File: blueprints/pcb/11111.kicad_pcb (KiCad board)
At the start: 2 copper layers, 128 parts, among them J1 MJ-4PP-9, J2 MJ-4PP-9, SW1 SW_Push, SW10 SW_Push, SW11 SW_Push, SW12 SW_Push, SW13 SW_Push, SW14 SW_Push, SW15 SW_Push, SW16 SW_Push, SW17 SW_Push, SW18 SW_Push, SW19 SW_Push, SW2 SW_Push, SW20 SW_Push, SW21 SW_Push, SW22 SW_Push, SW23 SW_Push, SW24 SW_Push, SW25 SW_Push, SW26 SW_Push, SW27 SW_Push, SW28 SW_Push, SW29 SW_Push, SW3 SW_Push, SW30 SW_Push, SW31 SW_Push, SW32 SW_Push, SW33 SW_Push, SW34 SW_Push, SW35 SW_Push, SW36 SW_Push, SW37 SW_Push, SW38 SW_Push, SW39 SW_Push, SW4 SW_Push, SW40 SW_Push, SW41 SW_Push, SW42 SW_Push, SW43 SW_Push, SW44 SW_Push, SW45 SW_Push, SW46 SW_Push, SW47 SW_Push, SW48 SW_Push, SW49 SW_Push, SW5 SW_Push, SW50 SW_Push, SW51 SW_Push, SW52 SW_Push, SW53 SW_Push, SW54 SW_Push, SW55 SW_Push, SW56 SW_Push, SW57 SW_Push, SW58 SW_Push, SW59 SW_Push, SW6 SW_Push, SW60 SW_Push, SW61 SW_Push, SW62 SW_Push, SW7 SW_Push, SW8 SW_Push, SW9 SW_Push

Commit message: edit PCB
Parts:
- moved SW28 267.6 mm to (281.9, 39.4)
- moved D28 259.7 mm to (269.8, 44.5), turned to 90 degrees
- moved D41 237.2 mm to (250.8, 63.5), turned to 90 degrees
- moved SW14 215.3 mm to (281.9, 20.3)
- moved SW56 211.5 mm to (281.9, 77.5)
- moved D10 200.0 mm to (193.6, 25.4), turned to 90 degrees
- moved D12 197.9 mm to (231.8, 26.3), turned to 90 degrees
- moved D14 195.5 mm to (270.2, 27.8), turned to 90 degrees
- moved D13 193.3 mm to (250.8, 25.4), turned to 90 degrees
- moved SW40 192.9 mm to (243.8, 58.4)
- moved SW13 192.6 mm to (262.8, 20.3)
- moved D24 185.7 mm to (193.7, 44.5), turned to 90 degrees
- moved D11 182.1 mm to (212.9, 26.3), turned to 90 degrees
- moved D39 181.1 mm to (212.7, 63.5), turned to 90 degrees
- moved D38 180.1 mm to (193.7, 63.5), turned to 90 degrees
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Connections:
- SW60 pad 1: Col11 -> Col7
- SW61 pad 1: Col12 -> Col8
- SW62 pad 1: Col13 -> Col9

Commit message: edit PCB
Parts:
- moved RZ2 57.6 mm to (213.2, 48.0), turned to 90 degrees
- moved D62 56.0 mm to (239.7, 123.2), turned to 180 degrees
- moved D61 55.4 mm to (220.6, 123.2), turned to 180 degrees
- moved D22 54.3 mm to (205.8, 66.4), turned to 180 degrees
- moved D60 51.7 mm to (201.9, 123.2), turned to 180 degrees
- moved D36 51.3 mm to (201.9, 85.5), turned to 180 degrees
- moved D41 51.2 mm to (297.2, 85.1), turned to 180 degrees
- moved D42 51.2 mm to (316.3, 85.1), turned to 180 degrees
- moved D37 51.0 mm to (220.6, 85.5), turned to 180 degrees
- moved D23 51.0 mm to (220.6, 66.4), turned to 180 degrees
- moved D52 51.0 mm to (239.7, 104.5), turned to 180 degrees
- moved D50 51.0 mm to (201.6, 104.5), turned to 180 degrees
- moved D24 51.0 mm to (239.7, 66.4), turned to 180 degrees
- moved D51 51.0 mm to (220.6, 104.5), turned to 180 degrees
- moved D53 51.0 mm to (258.7, 104.5), turned to 180 degrees
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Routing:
- net Col0: track 0.00 -> 202.0 mm, vias 0 -> 1
- net Row3: track 0.00 -> 196.6 mm, vias 0 -> 1
- net Row2: track 0.00 -> 181.0 mm, vias 0 -> 4
- net Col1: track 0.00 -> 180.8 mm, vias 0 -> 2
- net Row1: track 0.00 -> 161.4 mm
- net Row4: track 0.00 -> 159.8 mm, vias 0 -> 4
- net Col2: track 0.00 -> 155.7 mm, vias 0 -> 1
- net Row0: track 0.00 -> 148.9 mm, vias 0 -> 1
- net Col3: track 0.00 -> 133.0 mm, vias 0 -> 1
- net Col4: track 0.00 -> 121.1 mm, vias 0 -> 1
- net Col5: track 0.00 -> 104.5 mm, vias 0 -> 2
- net Col6: track 0.00 -> 88.7 mm, vias 0 -> 3
- net GND: track 0.00 -> 55.6 mm
- net VCC: track 0.00 -> 37.6 mm
- net DataLeft: track 0.00 -> 35.7 mm, vias 0 -> 3
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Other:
- board outline added: 298.5 x 99.1 mm

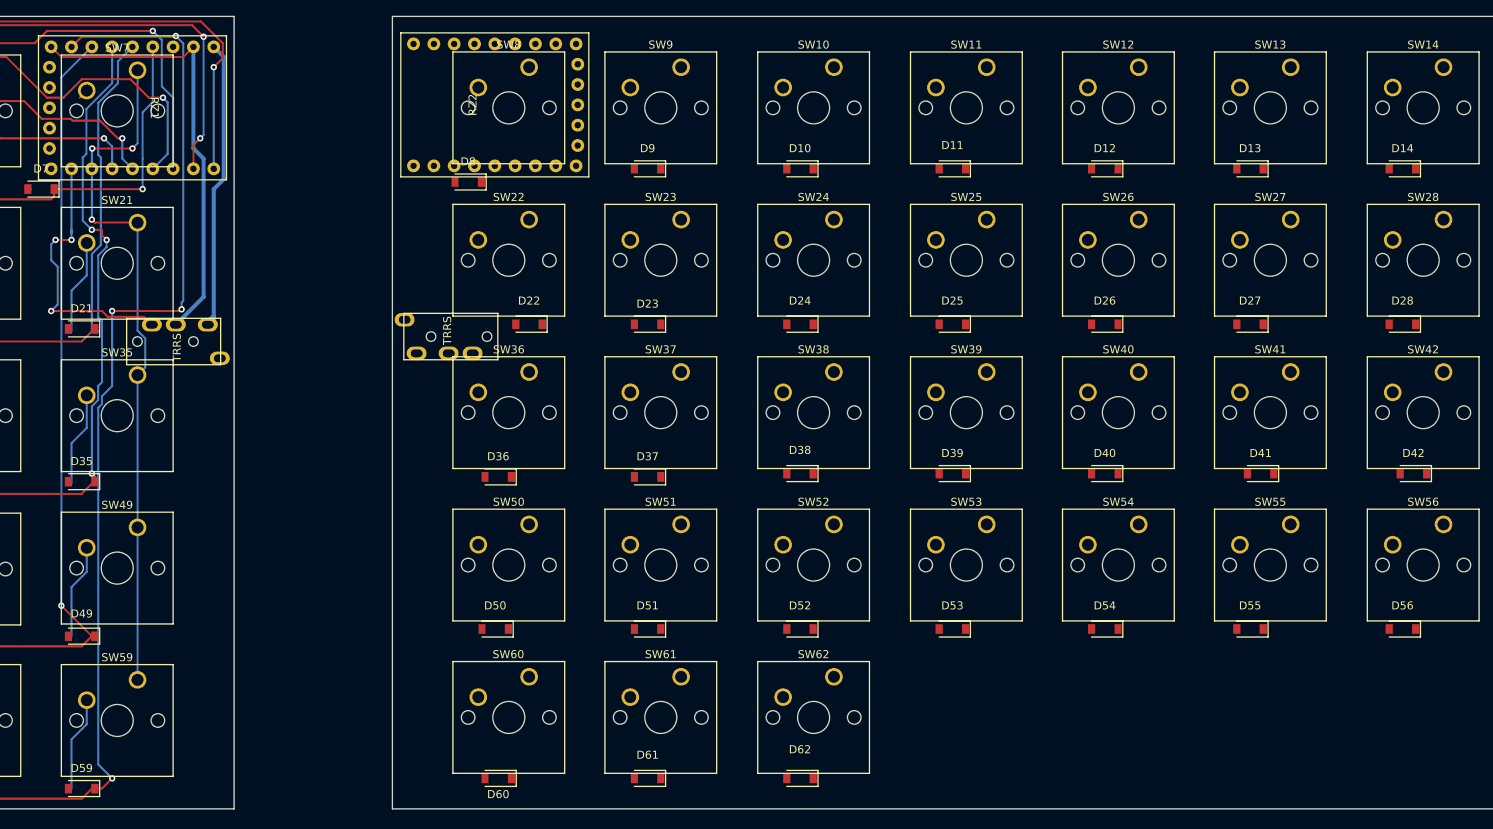
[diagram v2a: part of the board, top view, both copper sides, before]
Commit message: add Raspberry pi pico library
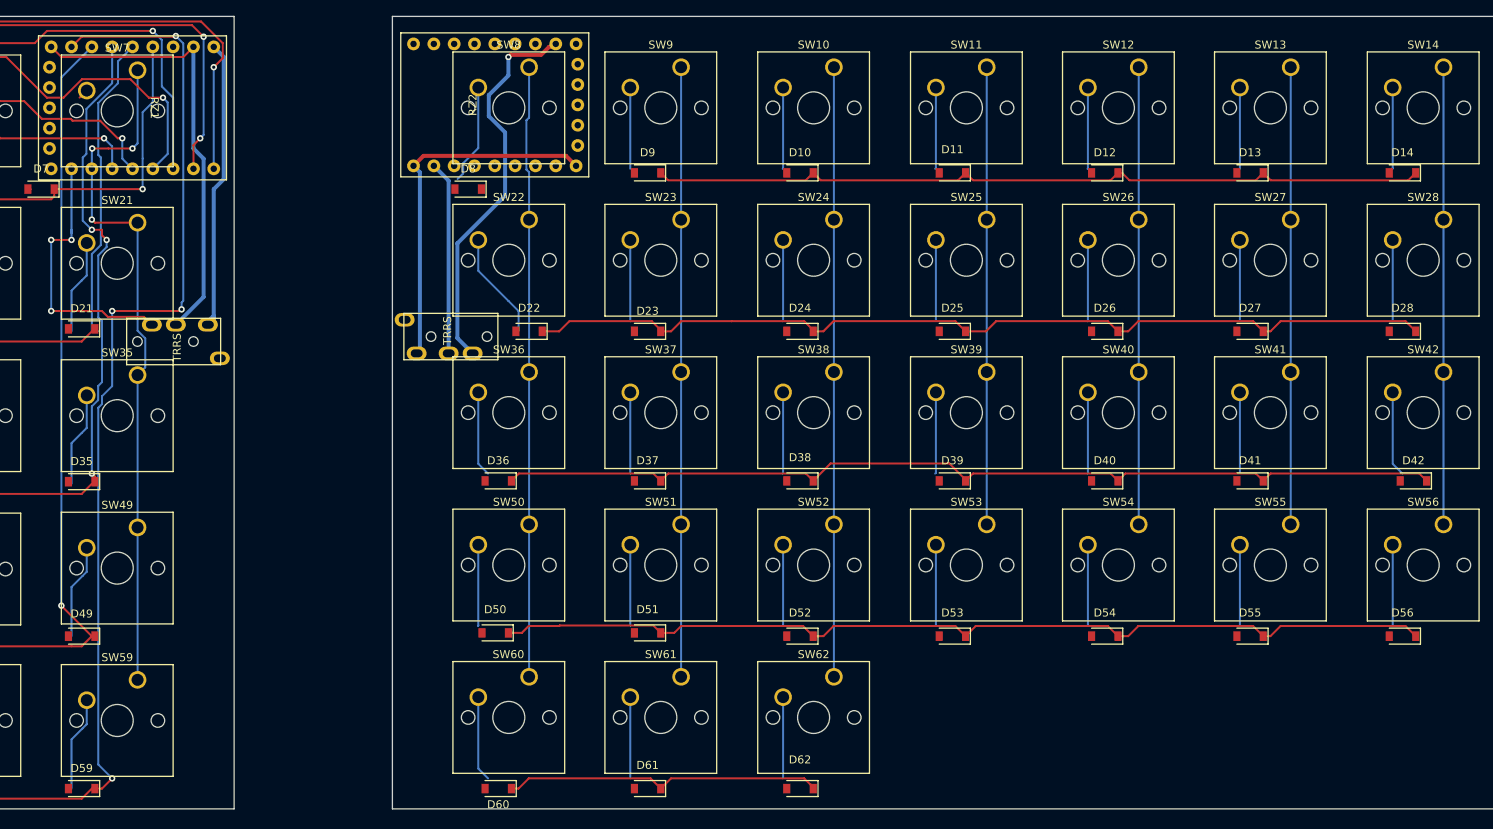
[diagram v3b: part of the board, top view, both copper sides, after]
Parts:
- moved D41 1.60 mm to (295.9, 86.0)
- moved D60 1.27 mm to (201.9, 124.5)
- moved D61 1.27 mm to (220.6, 124.5)
- moved D62 1.27 mm to (239.7, 124.5)
- moved D38 0.91 mm to (239.7, 86.0)
- moved D39 0.91 mm to (258.7, 86.0)
- moved D40 0.91 mm to (277.8, 86.0)
- moved D42 0.91 mm to (316.3, 86.0)
- moved D22 0.89 mm to (205.8, 67.3)
- moved D23 0.89 mm to (220.6, 67.3)
- moved D24 0.89 mm to (239.7, 67.3)
- moved D25 0.89 mm to (258.7, 67.3)
- moved D26 0.89 mm to (277.8, 67.3)
- moved D27 0.89 mm to (295.9, 67.3)
- moved D28 0.89 mm to (315.0, 67.3)
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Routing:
- net Row7: track 0.00 -> 120.1 mm
- net Row8: track 0.00 -> 119.3 mm
- net Row6: track 0.00 -> 115.7 mm
- net Row5: track 0.00 -> 98.2 mm
- net Col7: track 0.00 -> 76.5 mm
- net Col9: track 0.00 -> 76.2 mm
- net Col8: track 0.00 -> 76.2 mm
- net Col13: track 0.00 -> 57.1 mm
- net Col12: track 0.00 -> 57.1 mm
- net Col11: track 0.00 -> 57.1 mm
- net Col10: track 0.00 -> 57.1 mm
- net DataRight: track 0.00 -> 48.8 mm, vias 0 -> 1
- net VDD: track 0.00 -> 46.5 mm
- net Row9: track 0.00 -> 39.9 mm
- net GNDA: track 0.00 -> 24.2 mm
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
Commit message: update PCB, use Raspberry Pi Pico
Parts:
- removed RZ1, RZ2: RP2040-Zero, RP2040-zero:rp2040-zero
- added U1: Pico, Raspberry-pi-pico:RPi_Pico_SMD_TH, F.Cu at (55.9, 118.1)
- added U2: Pico, Raspberry-pi-pico:RPi_Pico_SMD_TH, F.Cu at (301.0, 118.1)
- J1, J2: value MJ-4PP-9 -> TRRS_MJ-4PP-9; footprint foostan:MJ-4PP-9_1side -> Salicylic-acid3_kbd_Parts:TRRS_MJ-4PP-9
- moved D7 7.73 mm to (152.4, 48.3)
- moved D22 6.30 mm to (212.1, 67.3)
- moved D21 4.96 mm to (145.2, 68.6)
- moved D8 3.61 mm to (201.6, 48.3)
- moved D59 2.54 mm to (152.4, 124.5)
- moved D45 1.65 mm to (75.3, 105.4)
- moved D33 1.65 mm to (113.4, 86.1)
- moved D47 1.65 mm to (113.4, 105.4)
- moved D17 1.43 mm to (74.9, 67.0)
- moved D31 1.43 mm to (74.9, 86.1)
- moved D48 1.27 mm to (132.1, 105.4)
- moved D35 1.27 mm to (151.1, 86.1)
- moved D49 1.27 mm to (151.1, 105.4)
- moved D34 0.89 mm to (132.1, 86.1)
- moved D10 0.76 mm to (239.7, 48.3)
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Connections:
- J1 pad B: DataLeft -> GND
- J1 pad C: GND -> DataLeft
- J2 pad B: DataRight -> GNDA
- J2 pad C: GNDA -> DataRight
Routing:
- net GND: track 55.6 -> 228.2 mm, vias 0 -> 1
- net DataLeft: track 35.3 -> 180.2 mm, vias 3 -> 1
- net VCC: track 37.6 -> 168.6 mm, vias 0 -> 4
- net Col0: track 202.0 -> 97.5 mm, vias 1 -> 2
- net Col1: track 180.8 -> 76.9 mm, vias 2 -> 0
- net Row4: track 159.8 -> 77.6 mm, vias 4 -> 0
- net Row0: track 148.9 -> 229.3 mm, vias 1 -> 3
- net Col6: track 88.7 -> 161.5 mm, vias 3 -> 1
- net Col2: track 155.7 -> 87.4 mm
- net Row3: track 196.6 -> 144.7 mm
- net DataRight: track 48.8 -> 0.00 mm, vias 1 -> 0
- net VDD: track 46.5 -> 0.00 mm
- net Col5: track 104.5 -> 144.7 mm, vias 2 -> 1
- net Row1: track 161.4 -> 198.0 mm, vias 0 -> 3
- net Col3: track 133.0 -> 102.5 mm, vias 1 -> 2
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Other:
- board size 298.5 x 99.1 mm -> 298.5 x 101.6 mm

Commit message: チェックエラーが0件になるまでPCB配線した
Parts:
- moved D30 2.65 mm to (57.1, 86.1)
- moved D3 2.54 mm to (76.2, 48.0)
- moved D19 2.54 mm to (114.3, 67.0)
- moved D57 2.54 mm to (114.3, 124.5)
- moved D58 2.54 mm to (133.3, 124.5)
- moved D29 2.22 mm to (37.7, 86.1)
- moved D20 1.78 mm to (133.0, 67.0)
- moved D6 1.78 mm to (133.0, 48.3)
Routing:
- net GNDA: track 0.00 -> 224.1 mm, vias 0 -> 2
- net VDD: track 0.00 -> 192.8 mm, vias 0 -> 2
- net DataRight: track 0.00 -> 177.3 mm, vias 0 -> 1
- net Col7: track 78.3 -> 186.5 mm, vias 0 -> 2
- net Col8: track 76.2 -> 159.6 mm, vias 0 -> 2
- net Col13: track 57.1 -> 132.9 mm, vias 0 -> 2
- net Row5: track 119.4 -> 186.2 mm, vias 0 -> 1
- net Col9: track 76.2 -> 136.2 mm, vias 0 -> 2
- net Col10: track 57.1 -> 114.6 mm, vias 0 -> 2
- net Col12: track 57.1 -> 112.8 mm, vias 0 -> 2
- net Row9: track 39.9 -> 89.2 mm, vias 0 -> 2
- net Row6: track 109.0 -> 158.1 mm, vias 0 -> 1
- net Col11: track 57.1 -> 93.7 mm
- net Row7: track 119.1 -> 150.0 mm, vias 0 -> 1
- net Row8: track 119.3 -> 123.1 mm
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
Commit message: reduce silkscreen warnings
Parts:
- moved D44 5.90 mm to (58.4, 101.0)
- moved D43 5.63 mm to (39.0, 101.0)
- moved D45 5.59 mm to (78.7, 101.0)
- moved D54 2.91 mm to (277.8, 102.5)
- moved D56 2.84 mm to (316.2, 102.9)
- moved D55 2.84 mm to (297.2, 102.9)
- moved D16 2.65 mm to (57.1, 67.0)
- moved D2 2.65 mm to (57.1, 48.0)
- moved D1 2.60 mm to (38.1, 48.0)
- moved D15 2.60 mm to (38.1, 67.0)
- moved D5 2.54 mm to (114.3, 48.3)
- moved D18 1.65 mm to (95.2, 67.0)
- moved D32 1.65 mm to (95.2, 86.1)
- moved D4 1.65 mm to (95.2, 48.0)
- moved D46 1.65 mm to (95.2, 105.4)
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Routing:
- net Col3: track 102.5 -> 113.4 mm
- net DataLeft: track 178.1 -> 188.0 mm
- net Net-(D44-A): track 14.8 -> 8.52 mm
- net Net-(D45-A): track 13.7 -> 8.55 mm
- net Row0: track 228.8 -> 224.3 mm
- net Row8: track 123.1 -> 127.6 mm
- net Net-(D43-A): track 12.6 -> 8.18 mm
- net GND: track 225.2 -> 229.2 mm
- net Col4: track 123.1 -> 126.6 mm, vias 2 -> 1
- net Row6: track 158.1 -> 160.8 mm
- net Net-(D50-A): track 12.8 -> 15.0 mm
- net Net-(D36-A): track 13.2 -> 15.3 mm
- net Row4: track 78.0 -> 80.0 mm
- net Row5: track 186.2 -> 188.2 mm
- net Col6: track 160.6 -> 158.6 mm, vias 1 -> 2
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
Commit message: オモテウラを間違えていたので修正
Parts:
- D1, D10, D11, D12, D13, D14, D15, D16, D17, D18, D19, D2, D20, D21, D22, D23, D24, D25, D26, D27, D28, D29, D3, D30, D31, D32, D33, D34, D35, D36, D37, D38, D39, D4, D40, D41, D42, D43, D44, D45, D46, D47, D48, D49, D5, D50, D51, D52, D53, D54, D55, D56, D57, D58, D59, D6, D60, D61, D62, D7, D8, D9: footprint Diode_SMD:D_SOD-123 -> Salicylic-acid3_kbd_Parts:Diode_SMD
- SW1, SW10, SW11, SW12, SW13, SW14, SW15, SW16, SW17, SW18, SW19, SW2, SW20, SW21, SW22, SW23, SW24, SW25, SW26, SW27, SW28, SW29, SW3, SW30, SW31, SW32, SW33, SW34, SW35, SW36, SW37, SW38, SW39, SW4, SW40, SW41, SW42, SW43, SW44, SW45, SW46, SW47, SW48, SW49, SW5, SW50, SW51, SW52, SW53, SW54, SW55, SW56, SW57, SW58, SW59, SW6, SW60, SW61, SW62, SW7, SW8, SW9: footprint Button_Switch_Keyboard:SW_Cherry_MX_1.00u_PCB -> Salicylic-acid3_kbd_SW:CherryMX_Solder_1u
- U1, U2: moved to B.Cu
- moved D21 20.3 mm to (161.4, 56.4), turned to 0 degrees
- moved J1 16.1 mm to (170.0, 62.0)
- moved D14 15.2 mm to (325.3, 37.1), turned to 0 degrees
- moved D27 15.0 mm to (306.2, 56.4), turned to 0 degrees
- moved D53 14.7 mm to (268.2, 94.2), turned to 0 degrees
- moved D11 14.7 mm to (268.2, 37.1), turned to 0 degrees
- moved D12 14.7 mm to (287.2, 37.1), turned to 0 degrees
- moved D52 14.6 mm to (249.1, 94.2), turned to 0 degrees
- moved D10 14.6 mm to (249.1, 37.1), turned to 0 degrees
- moved D62 14.6 mm to (249.1, 113.3), turned to 0 degrees
- moved D61 14.6 mm to (230.0, 113.3), turned to 0 degrees
- moved D9 14.6 mm to (230.0, 37.1), turned to 0 degrees
- moved D8 14.6 mm to (211.0, 37.1), turned to 0 degrees
- moved D6 14.6 mm to (142.3, 37.1), turned to 0 degrees
- moved D47 14.5 mm to (123.3, 94.0), turned to 0 degrees
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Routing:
- net DataRight: track 177.2 -> 117.0 mm
- net VDD: track 192.8 -> 140.6 mm, vias 2 -> 1
- net Row9: track 89.2 -> 136.6 mm, vias 2 -> 3
- net Row0: track 224.3 -> 185.7 mm, vias 3 -> 1
- net Row1: track 196.6 -> 162.0 mm, vias 3 -> 1
- net Col13: track 132.9 -> 98.9 mm, vias 2 -> 0
- net Col2: track 87.4 -> 121.1 mm, vias 1 -> 3
- net Col1: track 76.1 -> 108.7 mm, vias 0 -> 2
- net Col11: track 93.7 -> 117.8 mm, vias 0 -> 2
- net Row2: track 166.2 -> 142.3 mm
- net Col10: track 114.6 -> 137.4 mm
- net DataLeft: track 188.0 -> 165.5 mm
- net Col9: track 137.0 -> 157.9 mm, vias 2 -> 1
- net Col8: track 160.3 -> 180.7 mm, vias 2 -> 3
- net Col0: track 97.5 -> 116.8 mm, vias 2 -> 3
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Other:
- board size 298.5 x 101.6 mm -> 302.3 x 100.2 mm

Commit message: update PCB
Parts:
- added R1: 5.1k, Resistor_THT:R_Axial_DIN0204_L3.6mm_D1.6mm_P5.08mm_Vertical, F.Cu at (111.8, 38.1)
- added R2: 5.1k, Resistor_THT:R_Axial_DIN0204_L3.6mm_D1.6mm_P5.08mm_Vertical, F.Cu at (114.3, 38.1)
- added U3: ~, keyboard_parts:USB_type-C_dip_module_AE-USB2.0-TYPE-C, F.Cu at (99.1, 25.0)
- moved U2 9.54 mm to (308.0, 116.6), turned to 90 degrees
- moved U1 9.49 mm to (62.8, 116.6)
- moved SW29 8.58 mm to (46.4, 78.7)
- moved SW30 8.58 mm to (65.3, 78.7)
- moved SW31 8.58 mm to (84.5, 78.7)
- moved SW32 8.58 mm to (103.5, 78.7)
- moved SW33 8.58 mm to (122.6, 78.7)
- moved SW34 8.58 mm to (141.6, 78.7)
- moved SW35 8.58 mm to (160.7, 78.7)
- moved SW36 8.58 mm to (210.2, 78.7)
- moved SW37 8.58 mm to (229.2, 78.7)
- moved SW38 8.58 mm to (248.3, 78.7)
- moved SW39 8.58 mm to (267.4, 78.7)
- moved SW40 8.58 mm to (286.4, 78.7)
- moved SW41 8.58 mm to (305.4, 78.7)
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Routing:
- net DataRight: track 117.0 -> 184.3 mm, vias 1 -> 3
- net Row9: track 136.6 -> 77.5 mm, vias 3 -> 0
- net Col11: track 117.8 -> 80.4 mm
- net Row8: track 124.1 -> 160.1 mm, vias 0 -> 4
- net Row7: track 145.8 -> 178.1 mm, vias 1 -> 2
- net Col10: track 137.4 -> 105.7 mm, vias 2 -> 3
- net VDD: track 140.6 -> 170.8 mm, vias 1 -> 3
- net Row6: track 163.8 -> 193.7 mm, vias 1 -> 2
- net Col12: track 107.0 -> 79.3 mm, vias 2 -> 3
- net Row5: track 185.5 -> 211.2 mm, vias 1 -> 2
- net Col9: track 157.9 -> 133.9 mm, vias 1 -> 2
- net Col13: track 98.9 -> 116.9 mm, vias 0 -> 3
- net GND: track 221.0 -> 204.0 mm, vias 1 -> 5
- net Col8: track 180.7 -> 165.2 mm, vias 3 -> 4
- net Col0: track 116.8 -> 107.7 mm, vias 3 -> 2
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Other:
- board size 302.3 x 100.2 mm -> 301.3 x 112 mm
